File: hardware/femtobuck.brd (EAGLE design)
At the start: 10.2 x 37.5 mm, 16 parts

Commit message: Fixed changes from QC
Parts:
- C1, C2: device SparkFun-Capacitors:1206 -> SparkFun-Capacitors:1206-CAP
- U1: value (none) -> AL8805
- moved SJ2 0.13 mm to (8.38, 28.2)
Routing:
- net OUT-: track 12.9 -> 13.6 mm
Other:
- board text added: "(typ.)"
- board text added: "Units are inches"
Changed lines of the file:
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@@
 <grid distance="0.05" unitdist="inch" unit="inch" style="lines" multiple="1" display="yes" altdistance="0.005" altunitdist="inch" altunit="inch"/>
 <layers>
-<layer number="1" name="Top" color="4" fill="1" visible="no" active="yes"/>
+<layer number="1" name="Top" color="4" fill="1" visible="yes" active="yes"/>
 <layer number="2" name="Route2" color="1" fill="3" visible="no" active="yes"/>
 <layer number="15" name="Route15" color="4" fill="6" visible="no" active="yes"/>
@@
 <layer number="19" name="Unrouted" color="6" fill="1" visible="yes" active="yes"/>
 <layer number="20" name="Dimension" color="6" fill="1" visible="yes" active="yes"/>
-<layer number="21" name="tPlace" color="16" fill="1" visible="no" active="yes"/>
+<layer number="21" name="tPlace" color="16" fill="1" visible="yes" active="yes"/>
 <layer number="22" name="bPlace" color="14" fill="1" visible="yes" active="yes"/>
-<layer number="23" name="tOrigins" color="15" fill="1" visible="no" active="yes"/>
+<layer number="23" name="tOrigins" color="15" fill="1" visible="yes" active="yes"/>
 <layer number="24" name="bOrigins" color="15" fill="1" visible="yes" active="yes"/>
 <layer number="25" name="tNames" color="7" fill="1" visible="no" active="yes"/>
@@
 <layer number="43" name="vRestrict" color="2" fill="10" visible="no" active="yes"/>
 <layer number="44" name="Drills" color="7" fill="1" visible="no" active="yes"/>
-<layer number="45" name="Holes" color="7" fill="1" visible="no" active="yes"/>
+<layer number="45" name="Holes" color="7" fill="1" visible="yes" active="yes"/>
 <layer number="46" name="Milling" color="3" fill="1" visible="no" active="yes"/>
-<layer number="47" name="Measures" color="7" fill="1" visible="no" active="yes"/>
-<layer number="51" name="tDocu" color="6" fill="1" visible="no" active="yes"/>
+<layer number="47" name="Measures" color="7" fill="1" visible="yes" active="yes"/>
+<layer number="51" name="tDocu" color="6" fill="1" visible="yes" active="yes"/>
 <layer number="52" name="bDocu" color="7" fill="1" visible="no" active="no"/>
 <layer number="3" name="Route3" color="4" fill="3" visible="no" active="no"/>
@@
 <text x="8.763" y="28.956" size="1.27" layer="22" font="vector" ratio="15" rot="MR0" align="bottom-center">D+</text>
 <text x="6.096" y="28.448" size="0.8128" layer="22" font="vector" ratio="15" rot="SMR270">LED Driver</text>
+<dimension x1="0" y1="1.27" x2="0" y2="38.735" x3="-3.81" y3="20.0025" textsize="1.778" textratio="15" layer="47" dtype="vertical" unit="inch" precision="3"/>
+<dimension x1="0" y1="1.27" x2="10.16" y2="1.27" x3="5.08" y3="-2.54" textsize="1.778" textratio="15" layer="47" dtype="horizontal" unit="inch"/>
+<dimension x1="9.779" y1="7.366" x2="9.779" y2="4.064" x3="15.24" y3="5.715" textsize="1.778" textratio="15" layer="47" dtype="vertical" unit="inch" precision="3"/>
+<text x="14.605" y="16.51" size="1.778" layer="47" font="vector" ratio="15" rot="R90">(typ.)</text>
+<text x="0" y="-8.89" size="1.778" layer="47" font="vector" ratio="15">Units are inches</text>
 </plain>
 <attributes>
@@
 </class>
 </classes>
-<designrules name="Sparkfun">
+<designrules name="SparkFun-2-layer">
 <description language="en">&lt;b&gt;EAGLE Design Rules&lt;/b&gt;
 &lt;p&gt;
@@
 <param name="mdDrill" value="8mil"/>
 <param name="mdSmdStop" value="0mil"/>
-<param name="msWidth" value="8mil"/>
-<param name="msDrill" value="20mil"/>
+<param name="msWidth" value="7mil"/>
+<param name="msDrill" value="15mil"/>
 <param name="msMicroVia" value="9.99mm"/>
 <param name="msBlindViaRatio" value="0.5"/>
@@
 <param name="rlMinPadBottom" value="12mil"/>
 <param name="rlMaxPadBottom" value="20mil"/>
-<param name="rlMinViaOuter" value="10mil"/>
+<param name="rlMinViaOuter" value="7mil"/>
 <param name="rlMaxViaOuter" value="20mil"/>
-<param name="rlMinViaInner" value="10mil"/>
+<param name="rlMinViaInner" value="7mil"/>
 <param name="rlMaxViaInner" value="20mil"/>
 <param name="rlMinMicroViaOuter" value="4mil"/>
@@
 <param name="dpGapFactor" value="2.5"/>
 <param name="checkGrid" value="0"/>
-<param name="checkAngle" value="0"/>
+<param name="checkAngle" value="1"/>
 <param name="checkFont" value="1"/>
 <param name="checkRestrict" value="1"/>
@@
 </autorouter>
 <elements>
-<element name="U1" library="SparkFun-PowerIC" package="SOT23-5" value="" x="5.08" y="21.971">
+<element name="U1" library="SparkFun-PowerIC" package="SOT23-5" value="AL8805" x="5.08" y="21.971">
 <attribute name="PROD_ID" value="IC-11626" x="5.08" y="21.971" size="1.778" layer="27" display="off"/>
 <attribute name="VALUE" value="AL8805WS" x="5.08" y="21.971" size="1.778" layer="27" display="off"/>
@@
 <attribute name="VALUE" value="0.3" x="8.89" y="26.035" size="1.778" layer="27" rot="R90" display="off"/>
 </element>
-<element name="C1" library="SparkFun-Capacitors" package="1206" value="1uF" x="8.89" y="22.225" rot="R270">
-<attribute name="PROD_ID" value="CAP-09822" x="8.89" y="22.225" size="1.778" layer="27" rot="R270" display="off"/>
-<attribute name="VALUE" value="1.0uF" x="8.89" y="22.225" size="1.778" layer="27" rot="R270" display="off"/>
-</element>
-<element name="C2" library="SparkFun-Capacitors" package="1206" value="2.2uF" x="3.81" y="26.924" rot="R180">
-<attribute name="PROD_ID" value="CAP-10009" x="3.81" y="26.924" size="1.778" layer="27" rot="R180" display="off"/>
-<attribute name="VALUE" value="2.2UF" x="3.81" y="26.924" size="1.778" layer="27" rot="R180" display="off"/>
-</element>
+<element name="C1" library="SparkFun-Capacitors" package="1206-CAP" value="1uF" x="8.89" y="22.225" rot="R270"/>
+<element name="C2" library="SparkFun-Capacitors" package="1206-CAP" value="2.2uF" x="3.81" y="26.924" rot="R180"/>
 <element name="L1" library="SparkFun-Passives" package="SRN6045" value="33uH" x="5.08" y="16.51">
 <attribute name="PROD_ID" value="NDUC-11627" x="5.08" y="16.51" size="1.778" layer="27" display="off"/>
@@
 <attribute name="PROD_ID" value="RES-11622" x="7.366" y="26.035" size="1.778" layer="27" font="vector" ratio="15" rot="R270" display="off"/>
 </element>
-<element name="SJ2" library="SparkFun-Passives" package="PAD-JUMPER-2-NO_NO_SILK" value="NO Jumper" x="8.382" y="28.067"/>
+<element name="SJ2" library="SparkFun-Passives" package="PAD-JUMPER-2-NO_NO_SILK" value="NO Jumper" x="8.382" y="28.194"/>
 </elements>
 <signals>
@@
 <contactref element="JP1" pad="3"/>
 <wire x1="5.08" y1="20.6709" x2="5.08" y2="22.098" width="0.3048" layer="1"/>
-<wire x1="5.588" y1="26.162" x2="6.35" y2="26.797" width="0.3048" layer="16"/>
-<wire x1="6.35" y1="26.797" x2="6.35" y2="31.75" width="0.3048" layer="16"/>
+<wire x1="5.588" y1="26.162" x2="6.35" y2="26.924" width="0.3048" layer="16"/>
+<wire x1="6.35" y1="26.924" x2="6.35" y2="31.75" width="0.3048" layer="16"/>
 <via x="5.08" y="22.098" extent="1-16" drill="0.508"/>
-<wire x1="5.08" y1="22.098" x2="5.588" y2="22.352" width="0.3048" layer="16"/>
-<wire x1="5.588" y1="22.352" x2="5.588" y2="26.162" width="0.3048" layer="16"/>
+<wire x1="5.08" y1="22.098" x2="5.588" y2="22.606" width="0.3048" layer="16"/>
+<wire x1="5.588" y1="22.606" x2="5.588" y2="26.162" width="0.3048" layer="16"/>
 <polygon width="0.3048" layer="16" isolate="0.3048">
 <vertex x="0" y="33.02"/>
@@
 <vertex x="6.35" y="13.97"/>
 </polygon>
-<wire x1="7.205" y1="16.335" x2="7.205" y2="13.555" width="1.016" layer="1"/>
-<wire x1="7.205" y1="13.555" x2="5.08" y2="11.43" width="1.016" layer="1"/>
-<wire x1="5.08" y1="11.43" x2="3.556" y2="11.43" width="1.016" layer="1"/>
+<wire x1="7.205" y1="16.335" x2="7.205" y2="12.285" width="1.016" layer="1"/>
+<wire x1="6.35" y1="11.43" x2="3.556" y2="11.43" width="1.016" layer="1"/>
 <wire x1="3.556" y1="11.43" x2="3.1242" y2="10.9982" width="1.016" layer="1"/>
 <wire x1="3.1242" y1="9.271" x2="3.1242" y2="10.9982" width="1.016" layer="1"/>
@@
 <wire x1="3.1242" y1="9.271" x2="3.1242" y2="7.0358" width="1.016" layer="1"/>
 <wire x1="3.1242" y1="7.0358" x2="3.81" y2="6.35" width="1.016" layer="1"/>
+<wire x1="6.35" y1="11.43" x2="7.205" y2="12.285" width="1.016" layer="1"/>
 </signal>
 <signal name="OUT+">
@@
 <wire x1="6.223" y1="21.971" x2="7.112" y2="21.971" width="0.3048" layer="1"/>
 <via x="7.112" y="21.971" extent="1-16" drill="0.508"/>
-<wire x1="6.985" y1="21.971" x2="6.477" y2="21.971" width="0.3048" layer="16"/>
+<wire x1="7.112" y1="21.971" x2="6.477" y2="21.971" width="0.3048" layer="16"/>
 <wire x1="6.477" y1="21.971" x2="6.096" y2="22.352" width="0.3048" layer="16"/>
 <wire x1="6.096" y1="22.352" x2="6.096" y2="25.273" width="0.3048" layer="16"/>
@@
 <wire x1="8.509" y1="25.908" x2="8.89" y2="26.289" width="0.3048" layer="16"/>
 <wire x1="8.89" y1="26.289" x2="8.89" y2="31.75" width="0.3048" layer="16"/>
-<wire x1="6.985" y1="21.971" x2="7.112" y2="21.971" width="0" layer="19" extent="1-16"/>
 </signal>
 <signal name="N$1">
 <contactref element="R1" pad="2"/>
 <contactref element="SJ2" pad="2"/>
-<wire x1="8.832" y1="28.067" x2="8.832" y2="26.993" width="0.4064" layer="1"/>
+<wire x1="8.832" y1="28.194" x2="8.832" y2="26.993" width="0.4064" layer="1"/>
 <wire x1="8.832" y1="26.993" x2="8.89" y2="26.935" width="0.4064" layer="1"/>
 </signal>

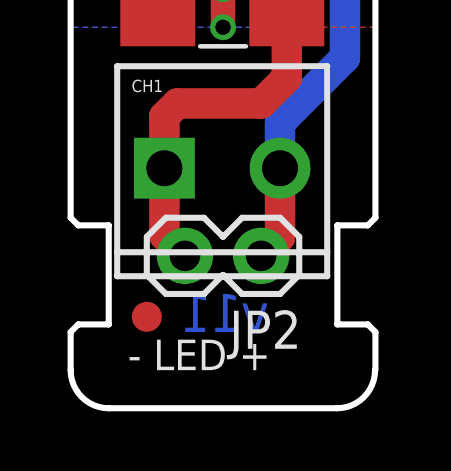
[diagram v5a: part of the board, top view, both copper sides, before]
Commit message: Chg to 12, inc. line wid on logos
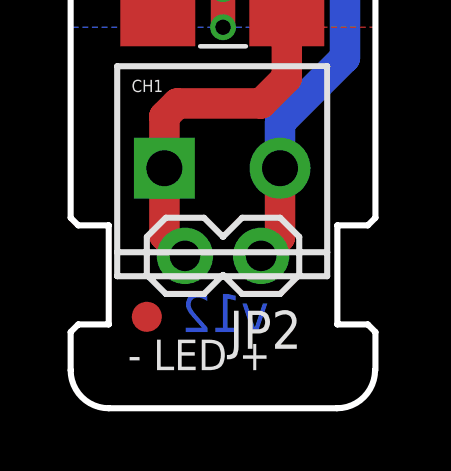
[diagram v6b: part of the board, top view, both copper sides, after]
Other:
- board text added: "v12"
- board text removed: "v11"
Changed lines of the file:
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@@
 <grid distance="0.05" unitdist="inch" unit="inch" style="lines" multiple="1" display="yes" altdistance="0.005" altunitdist="inch" altunit="inch"/>
 <layers>
-<layer number="1" name="Top" color="4" fill="1" visible="yes" active="yes"/>
+<layer number="1" name="Top" color="4" fill="1" visible="no" active="yes"/>
 <layer number="2" name="Route2" color="1" fill="3" visible="no" active="yes"/>
 <layer number="15" name="Route15" color="4" fill="6" visible="no" active="yes"/>
@@
 <layer number="19" name="Unrouted" color="6" fill="1" visible="yes" active="yes"/>
 <layer number="20" name="Dimension" color="6" fill="1" visible="yes" active="yes"/>
-<layer number="21" name="tPlace" color="16" fill="1" visible="yes" active="yes"/>
+<layer number="21" name="tPlace" color="16" fill="1" visible="no" active="yes"/>
 <layer number="22" name="bPlace" color="14" fill="1" visible="yes" active="yes"/>
-<layer number="23" name="tOrigins" color="15" fill="1" visible="yes" active="yes"/>
+<layer number="23" name="tOrigins" color="15" fill="1" visible="no" active="yes"/>
 <layer number="24" name="bOrigins" color="15" fill="1" visible="yes" active="yes"/>
 <layer number="25" name="tNames" color="7" fill="1" visible="no" active="yes"/>
@@
 <layer number="43" name="vRestrict" color="2" fill="10" visible="no" active="yes"/>
 <layer number="44" name="Drills" color="7" fill="1" visible="no" active="yes"/>
-<layer number="45" name="Holes" color="7" fill="1" visible="yes" active="yes"/>
+<layer number="45" name="Holes" color="7" fill="1" visible="no" active="yes"/>
 <layer number="46" name="Milling" color="3" fill="1" visible="no" active="yes"/>
-<layer number="47" name="Measures" color="7" fill="1" visible="yes" active="yes"/>
-<layer number="51" name="tDocu" color="6" fill="1" visible="yes" active="yes"/>
+<layer number="47" name="Measures" color="7" fill="1" visible="no" active="yes"/>
+<layer number="51" name="tDocu" color="6" fill="1" visible="no" active="yes"/>
 <layer number="52" name="bDocu" color="7" fill="1" visible="no" active="no"/>
 <layer number="3" name="Route3" color="4" fill="3" visible="no" active="no"/>
@@
 <layer number="54" name="bGND_GNDA" color="1" fill="9" visible="no" active="no"/>
 <layer number="56" name="wert" color="7" fill="1" visible="no" active="no"/>
+<layer number="57" name="tCAD" color="7" fill="1" visible="no" active="no"/>
+<layer number="59" name="tCarbon" color="7" fill="1" visible="no" active="no"/>
+<layer number="60" name="bCarbon" color="7" fill="1" visible="no" active="no"/>
+<layer number="90" name="Modules" color="5" fill="1" visible="no" active="no"/>
 <layer number="91" name="Nets" color="2" fill="1" visible="no" active="no"/>
 <layer number="92" name="Busses" color="1" fill="1" visible="no" active="no"/>
@@
 <layer number="97" name="Info" color="7" fill="1" visible="no" active="no"/>
 <layer number="98" name="Guide" color="6" fill="1" visible="no" active="no"/>
+<layer number="99" name="SpiceOrder" color="7" fill="1" visible="no" active="no"/>
 <layer number="100" name="Muster" color="7" fill="1" visible="no" active="no"/>
 <layer number="101" name="Patch_Top" color="12" fill="4" visible="no" active="no"/>
@@
 <layer number="127" name="_tValues" color="7" fill="1" visible="no" active="no"/>
 <layer number="128" name="_bValues" color="7" fill="1" visible="no" active="no"/>
+<layer number="129" name="Mask" color="7" fill="1" visible="yes" active="yes"/>
 <layer number="131" name="prix" color="7" fill="1" visible="no" active="no"/>
 <layer number="132" name="test" color="7" fill="1" visible="no" active="no"/>
 <layer number="144" name="Drill_legend" color="7" fill="1" visible="no" active="no"/>
+<layer number="150" name="Notes" color="7" fill="1" visible="yes" active="yes"/>
 <layer number="151" name="HeatSink" color="7" fill="1" visible="no" active="no"/>
 <layer number="152" name="_bDocu" color="7" fill="1" visible="no" active="no"/>
+<layer number="153" name="FabDoc1" color="7" fill="1" visible="yes" active="yes"/>
+<layer number="154" name="FabDoc2" color="7" fill="1" visible="yes" active="yes"/>
+<layer number="155" name="FabDoc3" color="7" fill="1" visible="yes" active="yes"/>
 <layer number="199" name="Contour" color="7" fill="1" visible="no" active="no"/>
 <layer number="200" name="200bmp" color="1" fill="10" visible="no" active="no"/>
@@
 <layer number="223" name="223bmp" color="24" fill="1" visible="no" active="no"/>
 <layer number="224" name="224bmp" color="25" fill="1" visible="no" active="no"/>
+<layer number="225" name="225bmp" color="7" fill="1" visible="yes" active="yes"/>
+<layer number="226" name="226bmp" color="7" fill="1" visible="yes" active="yes"/>
+<layer number="227" name="227bmp" color="7" fill="1" visible="yes" active="yes"/>
+<layer number="228" name="228bmp" color="7" fill="1" visible="yes" active="yes"/>
+<layer number="229" name="229bmp" color="7" fill="1" visible="yes" active="yes"/>
+<layer number="230" name="230bmp" color="7" fill="1" visible="yes" active="yes"/>
+<layer number="231" name="231bmp" color="7" fill="1" visible="yes" active="yes"/>
 <layer number="248" name="Housing" color="7" fill="1" visible="no" active="no"/>
 <layer number="249" name="Edge" color="7" fill="1" visible="no" active="no"/>
@@
 <layer number="251" name="SMDround" color="12" fill="11" visible="no" active="no"/>
 <layer number="254" name="cooling" color="7" fill="1" visible="no" active="no"/>
+<layer number="255" name="routoute" color="7" fill="1" visible="yes" active="yes"/>
 </layers>
 <board>
@@
 <text x="6.35" y="33.401" size="1.016" layer="21" font="vector" ratio="15" rot="R90" align="center-left">DGND</text>
 <text x="8.128" y="33.401" size="1.016" layer="21" font="vector" ratio="15" rot="R90" align="center-left">CTRL</text>
-<text x="6.604" y="4.445" size="1.27" layer="16" font="vector" ratio="15" rot="MR0" align="center-left">v11</text>
+<text x="6.604" y="4.445" size="1.27" layer="16" font="vector" ratio="15" rot="MR0" align="center-left">v12</text>
 <text x="2.032" y="24.003" size="1.6764" layer="22" font="vector" ratio="15" rot="SMR270" align="center-left">FemtoBuck</text>
 <text x="2.032" y="36.83" size="1.016" layer="22" font="vector" ratio="15" rot="SMR270" align="center-left">PGND</text>

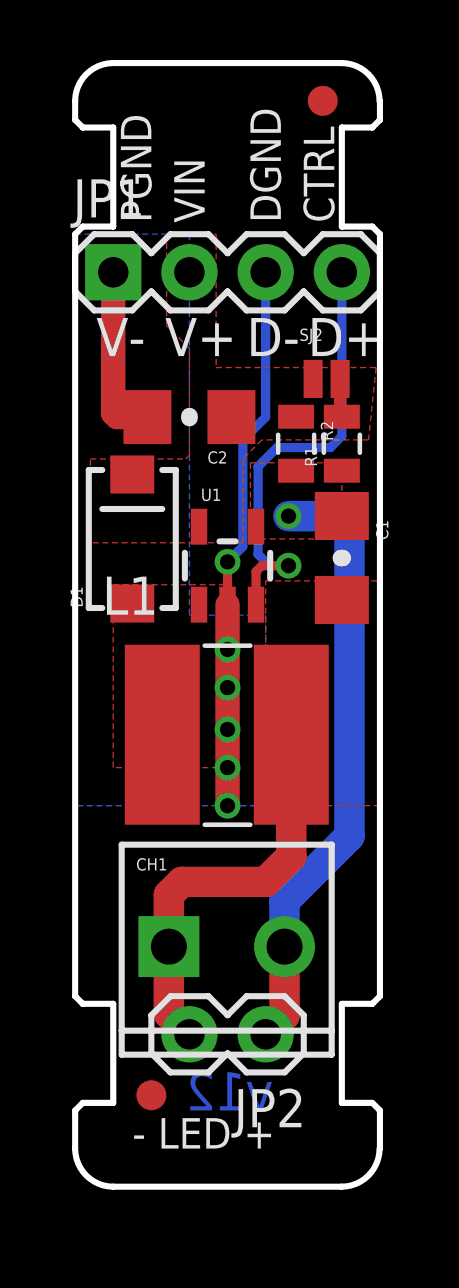
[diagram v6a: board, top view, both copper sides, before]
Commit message: AL8805 Buck LED driver EOL, replace with AL8860
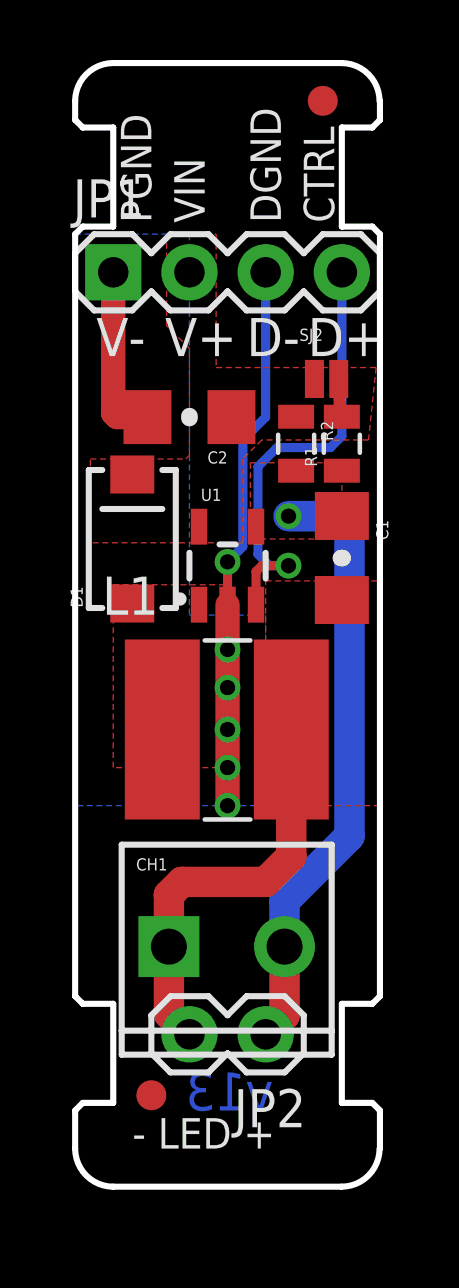
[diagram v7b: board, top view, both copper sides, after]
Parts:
- CH1: device SparkFun:SCREWTERMINAL-3.5MM-2_LOCK -> SparkFun-Connectors:SCREWTERMINAL-3.5MM-2_LOCK
- JP2: device SparkFun-Connectors:1X02 -> SparkFun-Connectors:1X02@1
- L1: value 33uH -> 33µH/±20%/1.4A; device SparkFun-Passives:SRN6045 -> SparkFun-Coils:SRN6045
- SJ2: device SparkFun-Passives:PAD-JUMPER-2-NO_NO_SILK -> SparkFun-Jumpers:SMT-JUMPER_2_NO_NO-SILK
- U1: value AL8805 -> AL8860; device SparkFun-PowerIC:SOT23-5 -> SparkFun-IC-Special-Function:SOT23-5
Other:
- board text added: "v13"
- board text removed: "v12"
